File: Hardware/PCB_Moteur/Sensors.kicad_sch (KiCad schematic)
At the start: 18 parts, among them J18 Screw_Terminal_01x04, J3 Screw_Terminal_01x04, U8 INA125UA/2K5, U9 MAX6612MXK

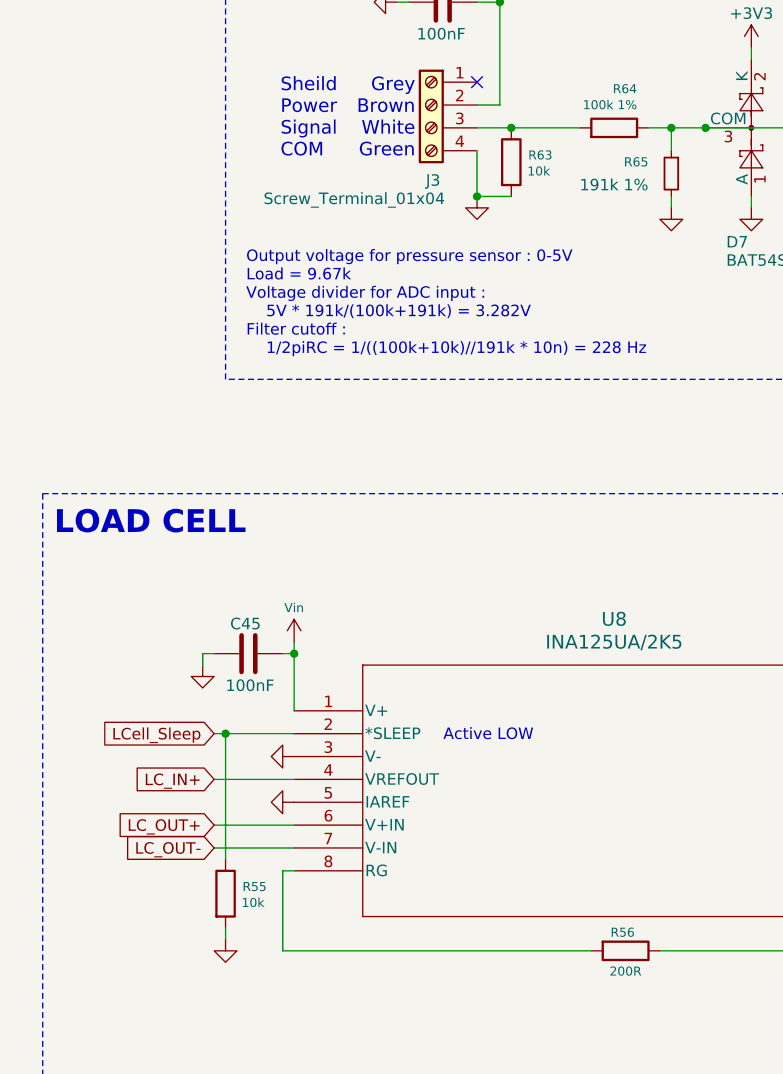
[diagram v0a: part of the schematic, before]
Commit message: wip : work on silkscreen and add all info to BOM
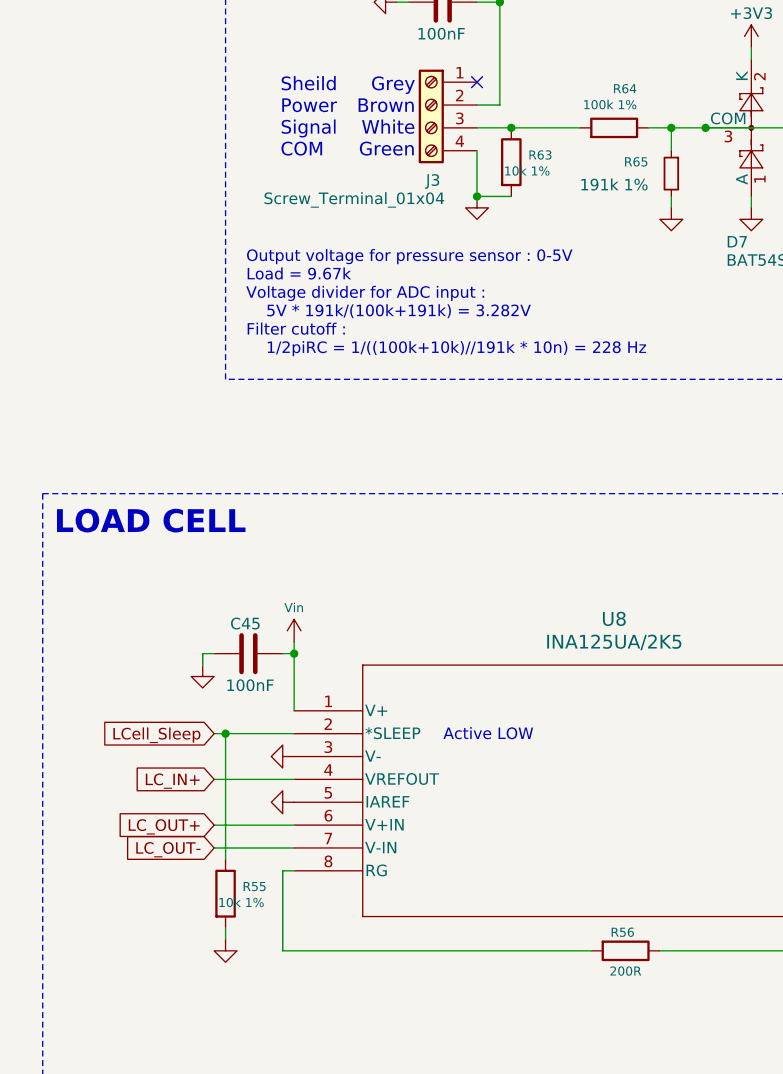
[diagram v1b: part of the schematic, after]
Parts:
- C45, C47, C48: DigiKey_Part_Number (none) -> 399-C0805C104K5RACTUCT-ND; Manufacturer_Part_Number (none) -> C0805C104K5RACTU
- C46: DigiKey_Part_Number (none) -> 399-C0603C103K5RACTUCT-ND; Manufacturer_Part_Number (none) -> C0603C103K5RACTU
- C56: footprint Capacitor_SMD:C_0603_1608Metric -> Capacitor_SMD:C_0805_2012Metric; DigiKey_Part_Number 399-C0603C104K3RACTUCT-ND -> 399-C0805C104K5RACTUCT-ND; Manufacturer_Part_Number C0603C104K3RACTU -> C0805C104K5RACTU
- C57: footprint Capacitor_SMD:C_0805_2012Metric -> Capacitor_SMD:C_0603_1608Metric; DigiKey_Part_Number 1276-2434-1-ND -> 399-C0603C103K5RACTUCT-ND; Manufacturer_Part_Number CL21B103KAANNNC -> C0603C103K5RACTU
- D6: DigiKey_Part_Number (none) -> 4878-BAT54SCT-ND; Manufacturer_Part_Number (none) -> BAT54S
- J18: DigiKey_Part_Number (none) -> ED10563-ND; Manufacturer_Part_Number (none) -> OSTVN04A150
- R55: value 10k -> 10k 1%; DigiKey_Part_Number (none) -> 541-10.0KCCT-ND; Manufacturer_Part_Number (none) -> CRCW080510K0FKEA
- R56: DigiKey_Part_Number (none) -> YAG3707CT-ND; Manufacturer_Part_Number (none) -> AC0805FR-07200RL
- R57: DigiKey_Part_Number (none) -> P1.5KDBCT-ND; Manufacturer_Part_Number (none) -> ERA-3AEB152V
- R63: value 10k -> 10k 1%; DigiKey_Part_Number 311-10.0KHRCT-ND -> 541-10.0KCCT-ND; Manufacturer_Part_Number RC0603FR-0710KL -> CRCW080510K0FKEA
- U8: DigiKey_Part_Number (none) -> 296-50343-1-ND; DigiKey_Part_Number  296-50343-1-ND -> (none)
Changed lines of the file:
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@@
 			)
 		)
-		(property "Datasheet" "https://www.diodes.com/assets/Datasheets/ds11005.pdf"
+		(property "Datasheet" "https://www.digikey.ca/en/products/detail/diotec-semiconductor/BAT54S/13164121"
 			(at 127 144.018 0)
 			(effects
@@
 			)
 		)
+		(property "DigiKey_Part_Number" "4878-BAT54SCT-ND"
+			(at 127 140.97 90)
+			(effects
+				(font
+					(size 1.27 1.27)
+				)
+				(hide yes)
+			)
+		)
+		(property "Manufacturer_Part_Number" "BAT54S"
+			(at 127 140.97 90)
+			(effects
+				(font
+					(size 1.27 1.27)
+				)
+				(hide yes)
+			)
+		)
 		(pin "1"
 		)
@@
 			)
 		)
-		(property "Datasheet" "~"
+		(property "Datasheet" "https://www.digikey.ca/en/products/detail/panasonic-electronic-components/ERA-3AEB152V/1465858"
 			(at 135.89 140.97 0)
 			(effects
@@
 		(property "Description" "Resistor, small symbol"
 			(at 135.89 140.97 0)
+			(effects
+				(font
+					(size 1.27 1.27)
+				)
+				(hide yes)
+			)
+		)
+		(property "DigiKey_Part_Number" "P1.5KDBCT-ND"
+			(at 135.89 140.97 90)
+			(effects
+				(font
+					(size 1.27 1.27)
+				)
+				(hide yes)
+			)
+		)
+		(property "Manufacturer_Part_Number" "ERA-3AEB152V"
+			(at 135.89 140.97 90)
 			(effects
 				(font
@@
 			)
 		)
-		(property "Datasheet" "~"
+		(property "Datasheet" "https://www.digikey.ca/en/products/detail/kemet/C0805C104K5RACTU/411169"
 			(at 262.89 34.29 0)
 			(effects
@@
 		(property "Description" "Unpolarized capacitor"
 			(at 262.89 34.29 0)
+			(effects
+				(font
+					(size 1.27 1.27)
+				)
+				(hide yes)
+			)
+		)
+		(property "DigiKey_Part_Number" "399-C0805C104K5RACTUCT-ND"
+			(at 262.89 34.29 90)
+			(effects
+				(font
+					(size 1.27 1.27)
+				)
+				(hide yes)
+			)
+		)
+		(property "Manufacturer_Part_Number" "C0805C104K5RACTU"
+			(at 262.89 34.29 90)
 			(effects
 				(font
@@
 			)
 		)
-		(property "Footprint" "Capacitor_SMD:C_0603_1608Metric"
+		(property "Footprint" "Capacitor_SMD:C_0805_2012Metric"
 			(at 62.23 47.9552 0)
 			(effects
@@
 			)
 		)
-		(property "Datasheet" "https://www.digikey.ca/en/products/detail/kemet/C0603C104K3RACTU/416044"
+		(property "Datasheet" "https://www.digikey.ca/en/products/detail/kemet/C0805C104K5RACTU/411169"
 			(at 58.42 46.99 0)
 			(effects
@@
 			)
 		)
-		(property "DigiKey_Part_Number" "399-C0603C104K3RACTUCT-ND"
+		(property "DigiKey_Part_Number" "399-C0805C104K5RACTUCT-ND"
 			(at 58.42 46.99 90)
 			(effects
@@
 			)
 		)
-		(property "Manufacturer_Part_Number" "C0603C104K3RACTU"
+		(property "Manufacturer_Part_Number" "C0805C104K5RACTU"
 			(at 58.42 46.99 90)
 			(effects
@@
 			)
 		)
-		(property "DigiKey_Part_Number " "296-50343-1-ND"
+		(property "Manufacturer_Part_Number" "INA125UA/2K5"
 			(at 41.91 125.73 0)
 			(effects
@@
 			)
 		)
-		(property "Manufacturer_Part_Number" "INA125UA/2K5"
+		(property "DigiKey_Part_Number" "296-50343-1-ND"
 			(at 41.91 125.73 0)
 			(effects
@@
 			)
 		)
-		(property "Datasheet" "~"
+		(property "Datasheet" "399-C0603C103K5RACTUCT-ND"
 			(at 257.81 44.45 0)
 			(effects
@@
 		)
 		(property "Description" "Unpolarized capacitor"
+			(at 257.81 44.45 0)
+			(effects
+				(font
+					(size 1.27 1.27)
+				)
+				(hide yes)
+			)
+		)
+		(property "DigiKey_Part_Number" "399-C0603C103K5RACTUCT-ND"
+			(at 257.81 44.45 0)
+			(effects
+				(font
+					(size 1.27 1.27)
+				)
+				(hide yes)
+			)
+		)
+		(property "Manufacturer_Part_Number" "C0603C103K5RACTU"
 			(at 257.81 44.45 0)
 			(effects
@@
 			)
 		)
-		(property "Datasheet" "~"
+		(property "Datasheet" "https://www.digikey.ca/en/products/detail/kemet/C0805C104K5RACTU/411169"
 			(at 142.24 144.78 0)
 			(effects
@@
 		)
 		(property "Description" "Unpolarized capacitor"
+			(at 142.24 144.78 0)
+			(effects
+				(font
+					(size 1.27 1.27)
+				)
+				(hide yes)
+			)
+		)
+		(property "DigiKey_Part_Number" "399-C0805C104K5RACTUCT-ND"
+			(at 142.24 144.78 0)
+			(effects
+				(font
+					(size 1.27 1.27)
+				)
+				(hide yes)
+			)
+		)
+		(property "Manufacturer_Part_Number" "C0805C104K5RACTU"
 			(at 142.24 144.78 0)
 			(effects
@@
 			)
 		)
-		(property "Datasheet" "~"
+		(property "Datasheet" "https://www.digikey.ca/en/products/detail/yageo/AC0805FR-07200RL/5896662"
 			(at 78.74 152.4 0)
 			(effects
@@
 					(size 1.27 1.27)
 				)
+			)
+		)
+		(property "DigiKey_Part_Number" "YAG3707CT-ND"
+			(at 78.74 152.4 90)
+			(effects
+				(font
+					(size 1.27 1.27)
+				)
+				(hide yes)
+			)
+		)
+		(property "Manufacturer_Part_Number" "AC0805FR-07200RL"
+			(at 78.74 152.4 90)
+			(effects
+				(font
+					(size 1.27 1.27)
+				)
+				(hide yes)
 			)
 		)
@@
 			)
 		)
-		(property "Footprint" "Capacitor_SMD:C_0805_2012Metric"
+		(property "Footprint" "Capacitor_SMD:C_0603_1608Metric"
 			(at 102.5652 68.58 0)
 			(effects
@@
 			)
 		)
-		(property "Datasheet" "https://www.digikey.ca/en/products/detail/samsung-electro-mechanics/CL21B103KAANNNC/3888092"
+		(property "Datasheet" "399-C0603C103K5RACTUCT-ND"
 			(at 101.6 64.77 0)
 			(effects
@@
 			)
 		)
-		(property "DigiKey_Part_Number" "1276-2434-1-ND"
+		(property "DigiKey_Part_Number" "399-C0603C103K5RACTUCT-ND"
 			(at 101.6 64.77 0)
 			(effects
@@
 			)
 		)
-		(property "Manufacturer_Part_Number" "CL21B103KAANNNC"
+		(property "Manufacturer_Part_Number" "C0603C103K5RACTU"
 			(at 101.6 64.77 0)
 			(effects
@@
 			)
 		)
+		(property "DigiKey_Part_Number" "ED10563-ND"
+			(at 132.08 110.49 0)
+			(effects
+				(font
+					(size 1.27 1.27)
+				)
+				(hide yes)
+			)
+		)
+		(property "Manufacturer_Part_Number" "OSTVN04A150"
+			(at 132.08 110.49 0)
+			(effects
+				(font
+					(size 1.27 1.27)
+				)
+				(hide yes)
+			)
+		)
 		(pin "1"
 		)
@@
 			)
 		)
-		(property "Value" "10k"
+		(property "Value" "10k 1%"
 			(at 38.608 147.066 0)
 			(effects
@@
 			)
 		)
-		(property "Datasheet" "~"
+		(property "Datasheet" "https://www.digikey.ca/en/products/detail/vishay-dale/CRCW080510K0FKEA/1175751"
 			(at 34.29 146.05 0)
 			(effects
@@
 					(size 1.27 1.27)
 				)
+			)
+		)
+		(property "DigiKey_Part_Number" "541-10.0KCCT-ND"
+			(at 34.29 146.05 0)
+			(effects
+				(font
+					(size 1.27 1.27)
+				)
+				(hide yes)
+			)
+		)
+		(property "Manufacturer_Part_Number" "CRCW080510K0FKEA"
+			(at 34.29 146.05 0)
+			(effects
+				(font
+					(size 1.27 1.27)
+				)
+				(hide yes)
 			)
 		)
@@
 			)
 		)
-		(property "Value" "10k"
+		(property "Value" "10k 1%"
 			(at 70.358 65.786 0)
 			(effects
@@
 			)
 		)
-		(property "Datasheet" "https://www.digikey.ca/en/products/detail/yageo/RC0603FR-0710KL/726880"
+		(property "Datasheet" "https://www.digikey.ca/en/products/detail/vishay-dale/CRCW080510K0FKEA/1175751"
 			(at 66.04 64.77 0)
 			(effects
@@
 			)
 		)
-		(property "DigiKey_Part_Number" "311-10.0KHRCT-ND"
+		(property "DigiKey_Part_Number" "541-10.0KCCT-ND"
 			(at 66.04 64.77 0)
 			(effects
@@
 			)
 		)
-		(property "Manufacturer_Part_Number" "RC0603FR-0710KL"
+		(property "Manufacturer_Part_Number" "CRCW080510K0FKEA"
 			(at 66.04 64.77 0)
 			(effects
@@
 			)
 		)
-		(property "Datasheet" "~"
+		(property "Datasheet" "https://www.digikey.ca/en/products/detail/kemet/C0805C104K5RACTU/411169"
 			(at 36.83 119.38 0)
 			(effects
@@
 			(effects
 				(font
+					(size 1.27 1.27)
+				)
+				(hide yes)
+			)
+		)
+		(property "DigiKey_Part_Number" "399-C0805C104K5RACTUCT-ND"
+			(at 36.83 119.38 90)
+			(effects
+				(font
+					(size 1.27 1.27)
+				)
+				(hide yes)
+			)
+		)
+		(property "Manufacturer_Part_Number" "C0805C104K5RACTU"
+			(at 36.83 119.38 90)
+			(effects
+				(font
